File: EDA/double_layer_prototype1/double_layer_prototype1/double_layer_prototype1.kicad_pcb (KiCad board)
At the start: 2 copper layers, 108 x 85.7 mm, 3 parts, among them U1 CD74HC4067SM, U2 CD74HC4067SM

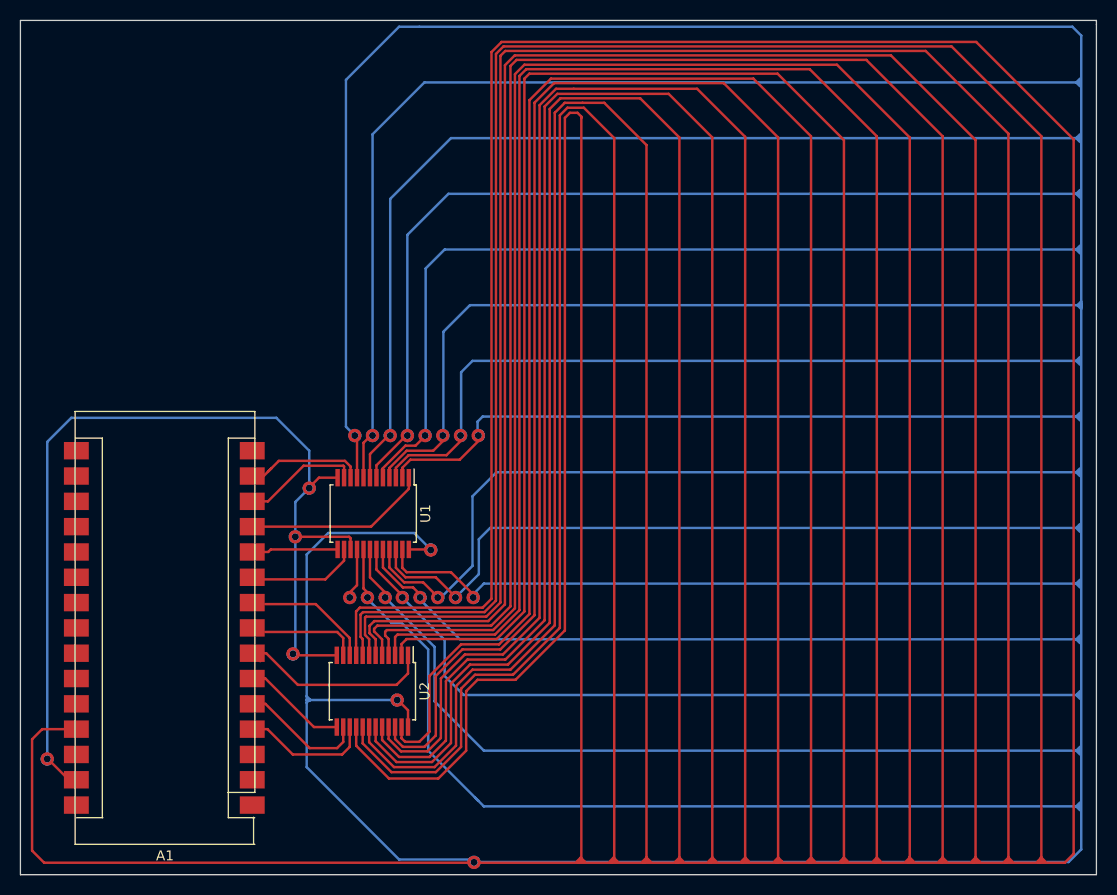
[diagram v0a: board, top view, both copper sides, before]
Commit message: update Arduino footprint
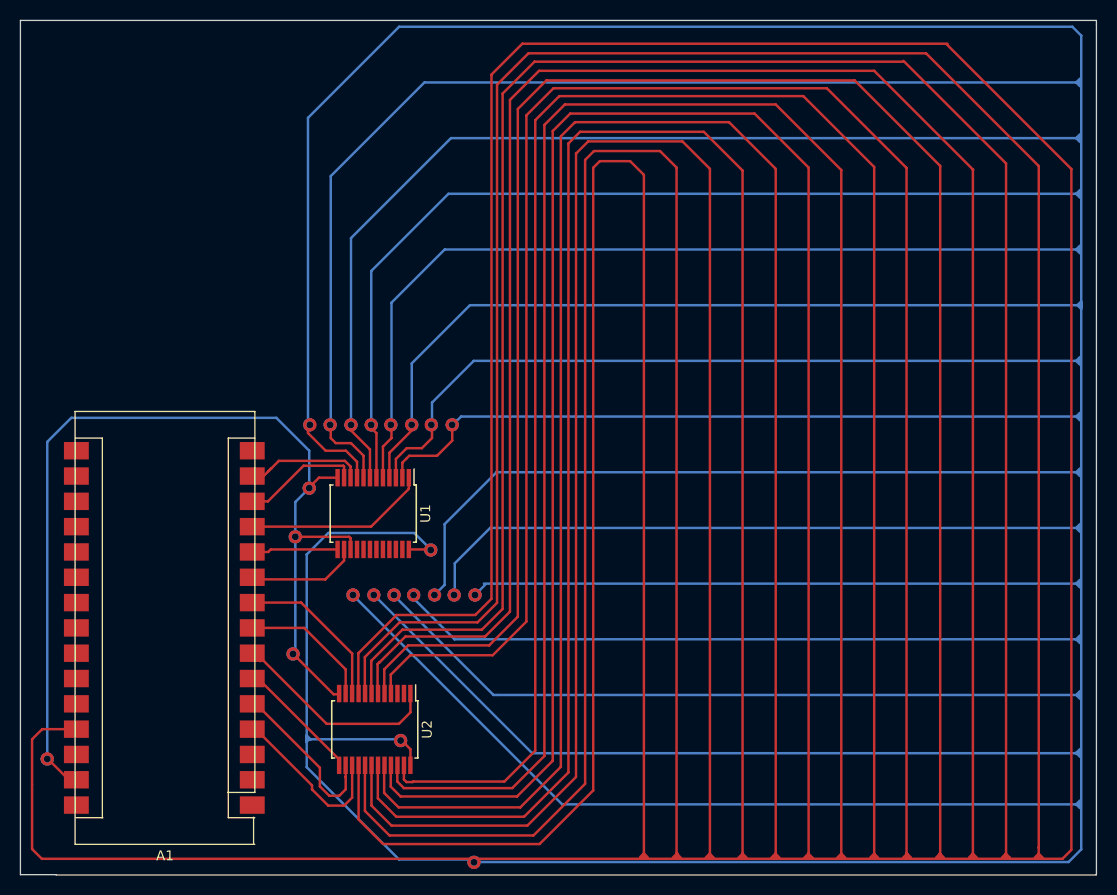
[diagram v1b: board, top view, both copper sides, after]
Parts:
- moved U2 3.84 mm to (80.6, 138.7)
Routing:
- net Net-(A1-Pad27): track 3115.2 -> 932.8 mm
- net unconnected-(U2-Pad5): track 0.00 -> 375.5 mm
- net unconnected-(U2-Pad2): track 0.00 -> 354.8 mm
- net unconnected-(U2-Pad9): track 0.00 -> 205.3 mm
- net unconnected-(U2-Pad8): track 0.00 -> 200.6 mm
- net unconnected-(U2-Pad7): track 0.00 -> 195.7 mm
- net unconnected-(U2-Pad3): track 0.00 -> 186.1 mm
- net unconnected-(U2-Pad4): track 0.00 -> 179.9 mm
- net unconnected-(U1-Pad8): track 1387.8 -> 1208.6 mm
- net unconnected-(U2-Pad16): track 0.00 -> 168.7 mm
- net (no net): track 0.00 -> 158.4 mm, vias 23 -> 22
- net unconnected-(U1-Pad23): track 9.78 -> 0.00 mm
- net unconnected-(U1-Pad22): track 8.39 -> 0.00 mm
- net unconnected-(U1-Pad9): track 0.00 -> 8.22 mm
- net unconnected-(U1-Pad21): track 7.26 -> 0.00 mm
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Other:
- board size 108 x 85.7 mm -> 108 x 85.8 mm
